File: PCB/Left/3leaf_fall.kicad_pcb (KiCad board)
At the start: 2 copper layers, 146.7 x 75.4 mm, 24 parts

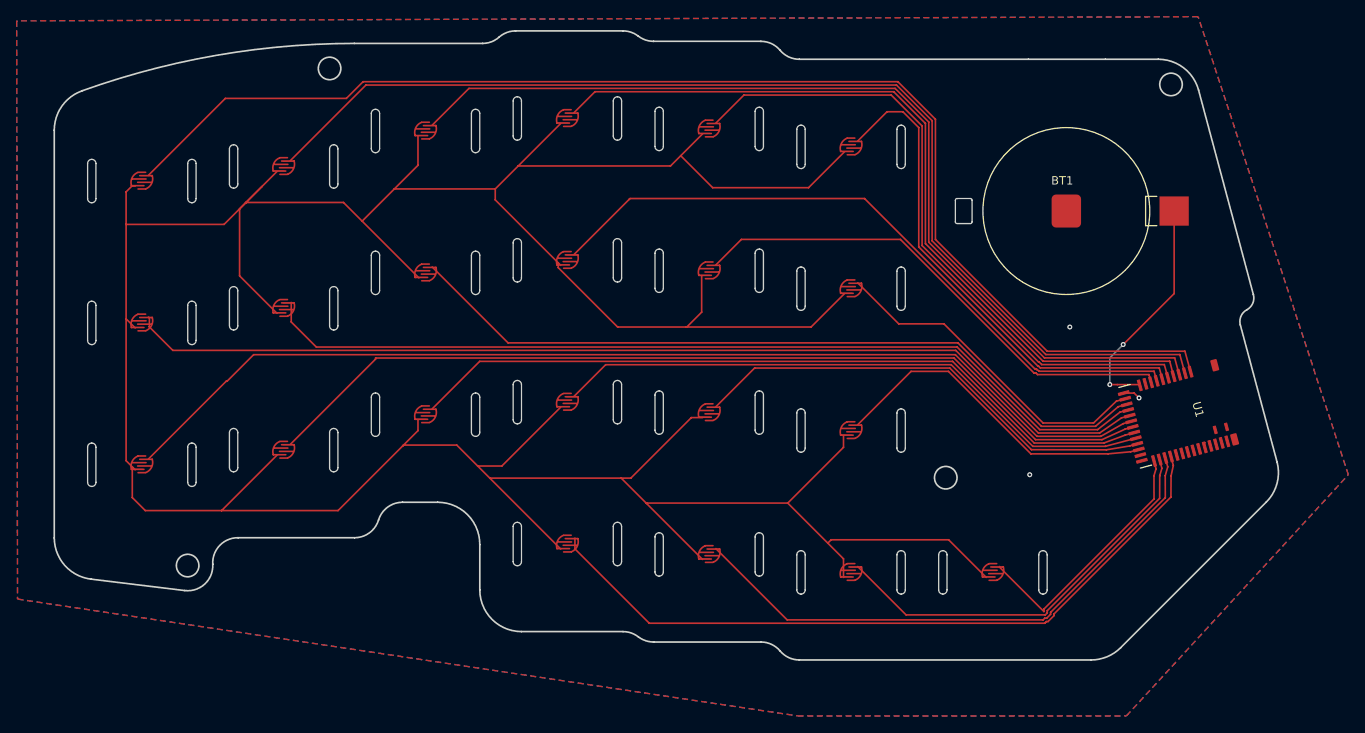
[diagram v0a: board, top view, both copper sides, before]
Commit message: Add TC-2030 interface; generate gerbers
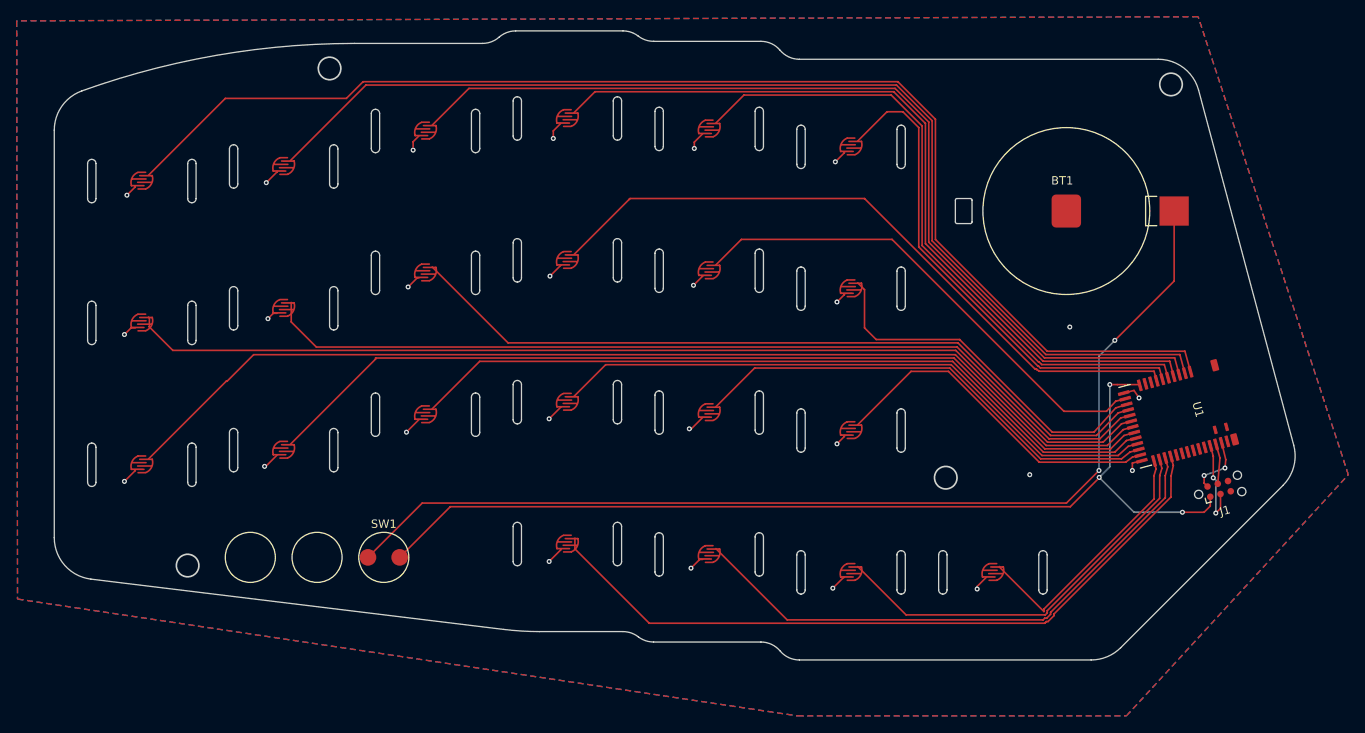
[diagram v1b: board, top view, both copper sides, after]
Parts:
- added J1: TC2030, Connector:Tag-Connect_TC2030-IDC-NL_2x03_P1.27mm_Vertical, F.Cu at (237.5, 95.6)
- added SW1: SW_Reed, keeblib:Magnet_reed_switch, F.Cu at (137.3, 103.8)
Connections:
- BT1 pad P: VCC -> Net-(BT1-PadP)
- U1 pad 13: S7 -> S8
- U1 pad 14: S10 -> S7
- U1 pad 15: S11 -> S10
- U1 pad 16: S12 -> S11
- U1 pad 17: S18 -> S12
- U1 pad 18: S17 -> S18
- U1 pad 19: S16 -> S17
- U1 pad 20: S15 -> S16
- U1 pad 21: S14 -> S15
- U1 pad 22: S13 -> S14
- U1 pad 23: unconnected-(U1-P0.10-Pad23) -> S13
- U1 pad 35: unconnected-(U1-P0.21/RESET-Pad35) -> RESET
- U1 pad 9: S8 -> unconnected-(U1-DEC4-Pad9)
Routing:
- net GND: track 436.8 -> 44.4 mm, vias 3 -> 26
- net Net-(BT1-PadP): track 0.00 -> 126.9 mm, vias 0 -> 2
- net VCC: track 27.7 -> 119.6 mm, vias 2 -> 3
- net RESET: track 0.00 -> 10.8 mm, vias 0 -> 2
- net SWD: track 0.00 -> 7.22 mm, vias 0 -> 2
- net SWC: track 0.00 -> 4.80 mm
- net S7: track 40.1 -> 43.7 mm
- net S8: track 60.8 -> 59.4 mm
- net S16: track 90.8 -> 91.8 mm
- net S17: track 109.7 -> 110.7 mm
- net S18: track 127.5 -> 128.5 mm
- net S12: track 124.6 -> 125.6 mm
- net S15: track 73.1 -> 74.1 mm
- net S11: track 108.8 -> 109.7 mm
- net S10: track 92.1 -> 93.0 mm
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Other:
- board size 146.7 x 75.4 mm -> 148.7 x 75.4 mm
